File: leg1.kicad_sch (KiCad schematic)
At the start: 12 parts, among them J2 Leg1 Motor1, J3 Leg1 Motor2, J4 Leg1 Motor3

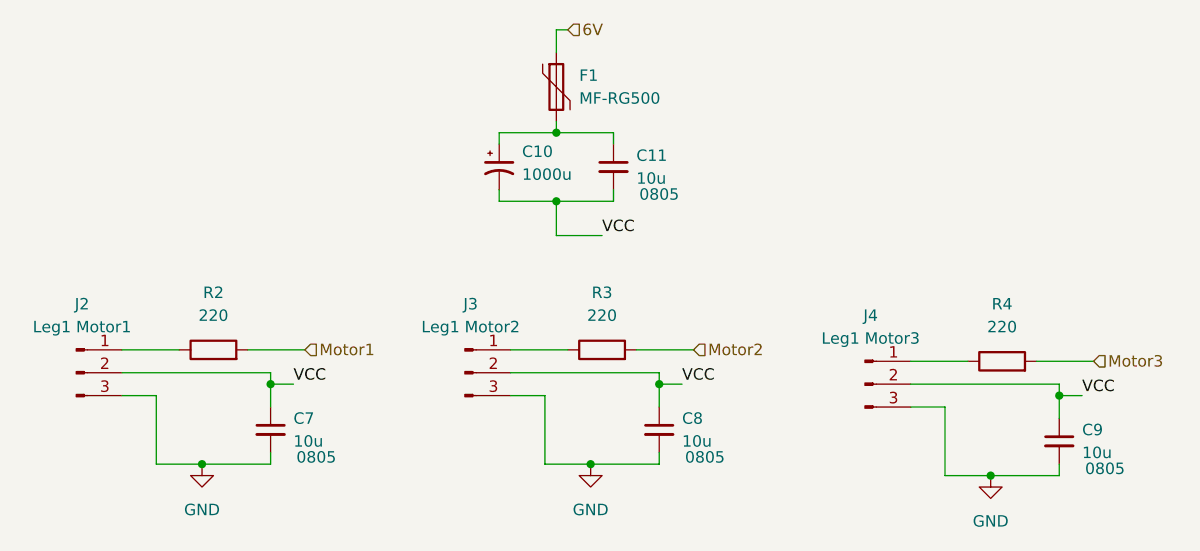
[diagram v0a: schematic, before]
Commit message: removed crystal, fixed caps
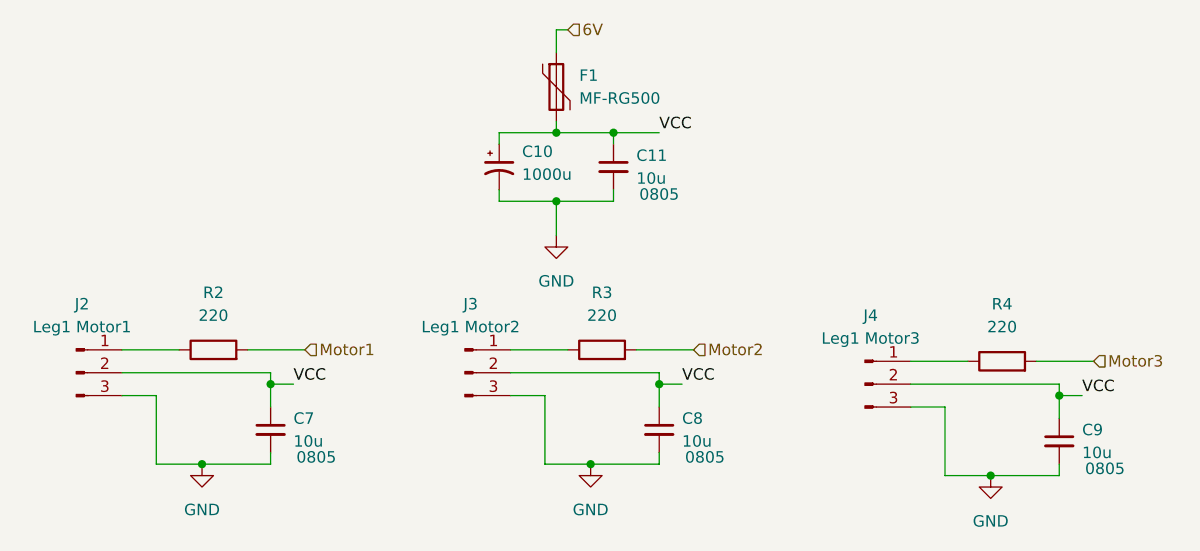
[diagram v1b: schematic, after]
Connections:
- net GND: now also C10.2, C11.2
- net VCC: now also C10.1, C11.1, F1.2; no longer C10.2, C11.2
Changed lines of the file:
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@@
+	)
+	(junction
+		(at 132.08 55.88)
+		(diameter 0)
+		(color 0 0 0 0)
 	)
 	(junction
@@
 	(wire
 		(pts
+			(xy 132.08 55.88) (xy 137.16 55.88)
+		)
+		(stroke
+			(width 0)
+			(type default)
+		)
+	)
+	(wire
+		(pts
 			(xy 81.28 85.09) (xy 77.47 85.09)
 		)
@@
 		(pts
 			(xy 132.08 55.88) (xy 132.08 57.15)
-		)
-		(stroke
-			(width 0)
-			(type default)
-		)
-	)
-	(wire
-		(pts
-			(xy 125.73 67.31) (xy 130.81 67.31)
 		)
 		(stroke
@@
 	)
 	(label "VCC"
-		(at 139.7 83.82 0)
+		(at 137.16 55.88 0)
 		(effects
 			(font
@@
 	)
 	(label "VCC"
-		(at 130.81 67.31 0)
+		(at 139.7 83.82 0)
 		(effects
 			(font
@@
 					(unit 1)
 				)
+			)
+		)
+	)
+	(symbol
+		(lib_id "power:GND")
+		(at 125.73 67.31 0)
+		(unit 1)
+		(exclude_from_sim no)
+		(in_bom yes)
+		(on_board yes)
+		(dnp no)
+		(property "Reference" "#PWR048"
+			(at 125.73 73.66 0)
+			(effects
+				(font
+					(size 1.27 1.27)
+				)
+				(hide yes)
+			)
+		)
+		(property "Value" "GND"
+			(at 125.73 72.39 0)
+			(effects
+				(font
+					(size 1.27 1.27)
+				)
+			)
+		)
+		(property "Footprint" ""
+			(at 125.73 67.31 0)
+			(effects
+				(font
+					(size 1.27 1.27)
+				)
+				(hide yes)
+			)
+		)
+		(property "Datasheet" ""
+			(at 125.73 67.31 0)
+			(effects
+				(font
+					(size 1.27 1.27)
+				)
+				(hide yes)
+			)
+		)
+		(property "Description" "Power symbol creates a global label with name \"GND\" , ground"
+			(at 125.73 67.31 0)
+			(effects
+				(font
+					(size 1.27 1.27)
+				)
+				(hide yes)
+			)
+		)
+		(pin "1"
+		)
+		(instances
+			(project "Project-Star"
+				(path "/dfa3d008-01ec-4328-886a-a4a57a49a859/86953d96-531f-4827-9448-d0cac3541dc1/73636b36-e11b-4bbb-a8ef-31dc5b9ed039"
+					(reference "#PWR048")
+					(unit 1)
+				)
